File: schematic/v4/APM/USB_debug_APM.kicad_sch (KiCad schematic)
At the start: 16 parts, among them J29 USB_A, J30 UART_DEBUG, U38 CH340G, Y7 12MHz

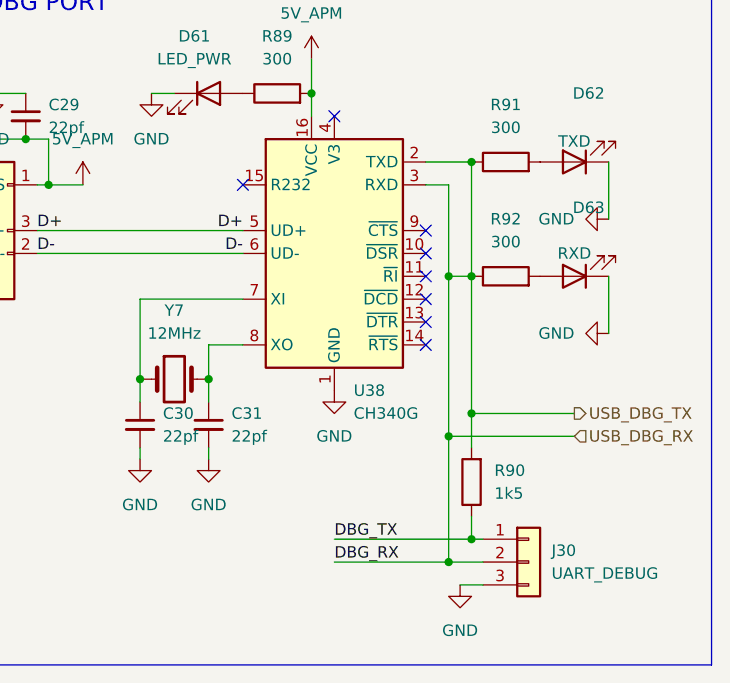
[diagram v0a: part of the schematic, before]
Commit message: ready for fab?
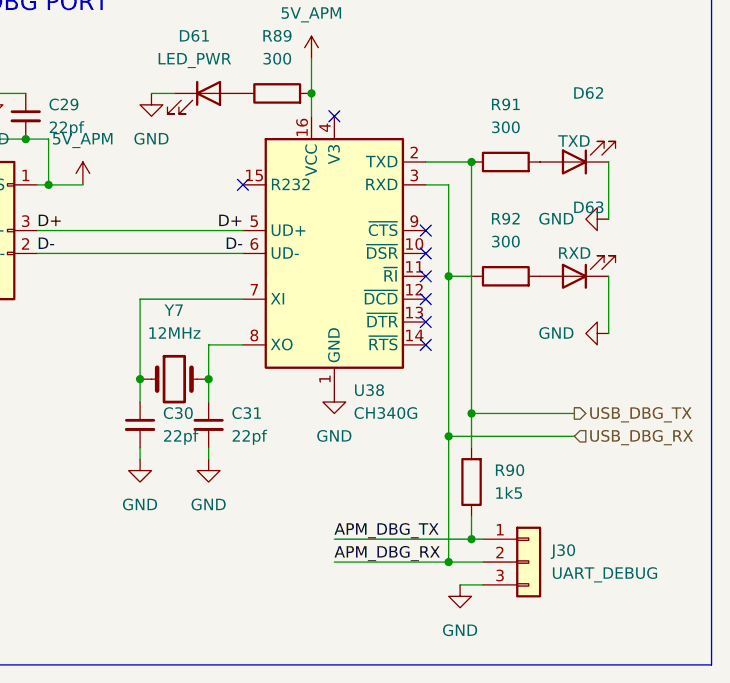
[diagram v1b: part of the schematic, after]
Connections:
- net USB_DBG_RX: no longer R90.2, R91.1, U38.2 (TXD)
- net DBG_TX renamed APM_DBG_TX
- new net USB_DBG_TX: R90.2, R91.1, U38.2 (TXD)
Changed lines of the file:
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@@
-	)
-	(junction
-		(at 171.45 83.82)
-		(diameter 0)
-		(color 0 0 0 0)
 	)
 	(junction
@@
 	(wire
 		(pts
-			(xy 171.45 83.82) (xy 171.45 99.06)
-		)
-		(stroke
-			(width 0)
-			(type default)
-		)
-	)
-	(wire
-		(pts
 			(xy 123.19 81.28) (xy 146.05 81.28)
 		)
@@
 	(wire
 		(pts
-			(xy 171.45 71.12) (xy 171.45 83.82)
+			(xy 171.45 71.12) (xy 171.45 99.06)
 		)
 		(stroke
@@
 		)
 	)
-	(label "DBG_RX"
+	(label "APM_DBG_RX"
 		(at 156.21 115.57 0)
 		(effects
@@
 		)
 	)
-	(label "DBG_TX"
+	(label "APM_DBG_TX"
 		(at 156.21 113.03 0)
 		(effects

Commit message: should be good for refab and actual layout. may need better BOM matching tho
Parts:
- J30: footprint Connector_PinHeader_1.00mm:PinHeader_1x03_P1.00mm_Horizontal -> Connector_PinHeader_2.54mm:PinHeader_1x03_P2.54mm_Horizontal
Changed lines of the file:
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@@
 			)
 		)
-		(property "Footprint" "Connector_PinHeader_1.00mm:PinHeader_1x03_P1.00mm_Horizontal"
+		(property "Footprint" "Connector_PinHeader_2.54mm:PinHeader_1x03_P2.54mm_Horizontal"
 			(at 177.8 115.57 0)
 			(effects
